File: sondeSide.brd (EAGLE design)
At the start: 127 x 31.8 mm, 33 parts

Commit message: I think its done, just needs labels
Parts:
- moved R2 6.37 mm to (42.4, 25.9), turned to 180 degrees
- moved R1 3.14 mm to (42.4, 23.4), turned to 180 degrees
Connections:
- net 3.3V: now also JP15.1
- net 5V: no longer U$1.UGND1, U$1.UGND2
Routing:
- net TX3: track 0.00 -> 68.8 mm
- net RX2: track 0.00 -> 63.0 mm
- net TX2: track 0.00 -> 62.5 mm
- net RX3: track 0.00 -> 61.0 mm
- net SCL: track 0.00 -> 54.3 mm
- net SDA: track 0.00 -> 50.7 mm
- net 3.3V: track 0.00 -> 32.7 mm
- net 12V: track 0.00 -> 27.5 mm

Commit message: I think its done
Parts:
- renumbered JP25 to VIN
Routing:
- net 3.3V: track 32.7 -> 105.5 mm
- net SCL: track 54.3 -> 40.7 mm
- net SDA: track 50.7 -> 51.2 mm
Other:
- board text added: "12V"
- board text added: "3.3V"
- board text added: "5V"
- board text added: "DEPTH"
- board text added: "GND"
- board text added: "RADIO"
- board text added: "RX"
- board text added: "RX2"
- board text added: "RX3"
- board text added: "SCL"
- board text added: "SDA"
- board text added: "SONDE"
- board text added: "TX"
- board text added: "TX2"
- board text added: "TX3"
- board text added: "V1 OCT 2018"

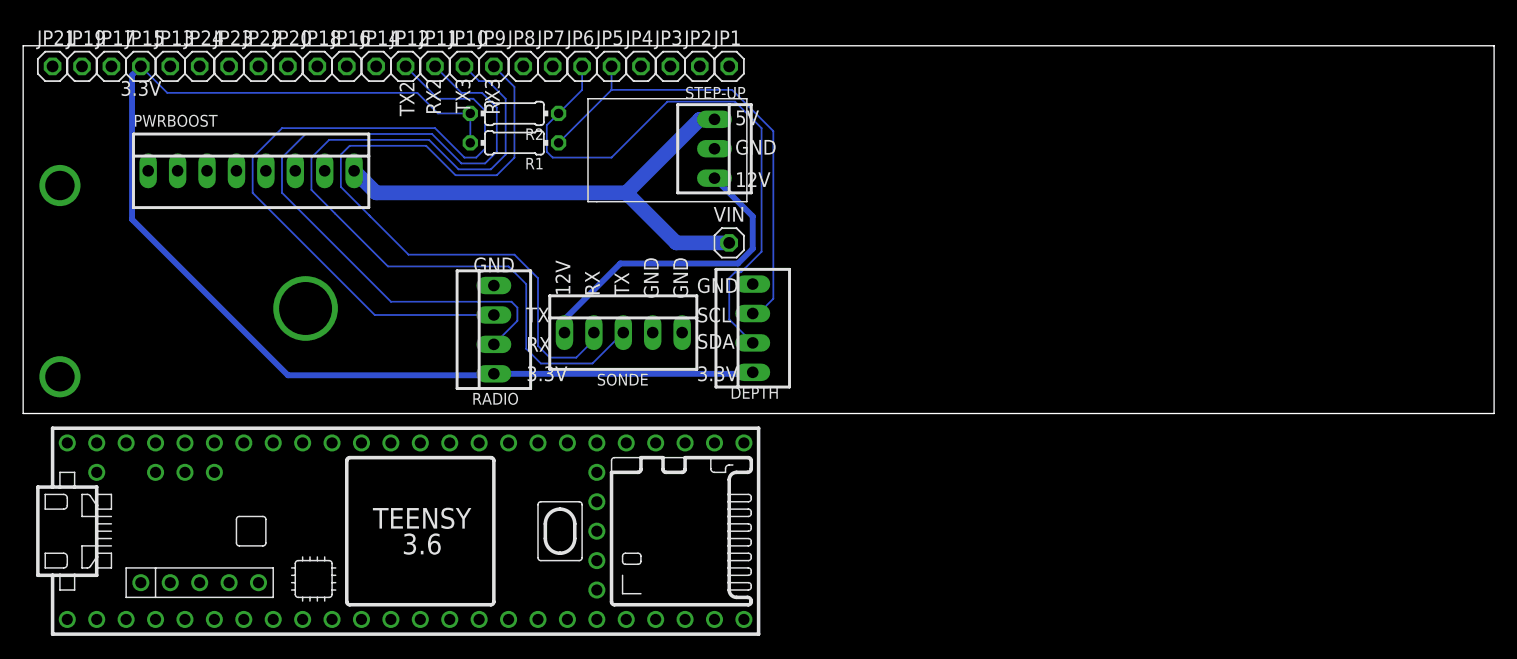
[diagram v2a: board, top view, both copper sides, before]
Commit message: Without external 3.3v step down
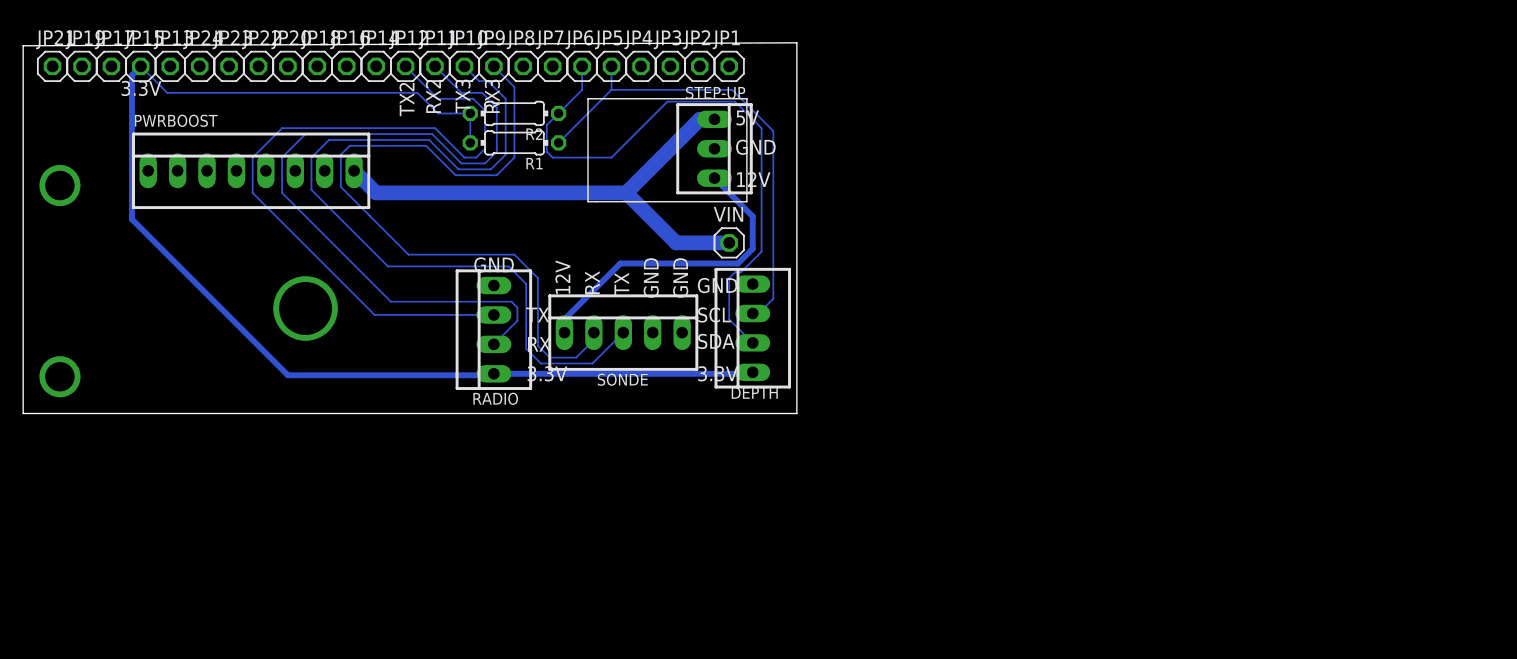
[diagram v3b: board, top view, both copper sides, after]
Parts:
- removed U$1: TEENSY_3.5/3.6, Teensy356:TEENSY_3.5/3.6
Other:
- board size 127 x 31.8 mm -> 66.8 x 32 mm
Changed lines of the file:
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@@
 <board>
 <plain>
-<wire x1="0" y1="0" x2="127" y2="0" width="0" layer="20"/>
-<wire x1="127" y1="0" x2="127" y2="31.75" width="0" layer="20"/>
-<wire x1="127" y1="31.75" x2="0" y2="31.75" width="0" layer="20"/>
+<wire x1="0" y1="0" x2="66.802" y2="0" width="0" layer="20"/>
+<wire x1="66.802" y1="0" x2="66.802" y2="32.004" width="0" layer="20"/>
+<wire x1="66.802" y1="32.004" x2="0" y2="31.75" width="0" layer="20"/>
 <wire x1="0" y1="31.75" x2="0" y2="0" width="0" layer="20"/>
 <wire x1="36.83" y1="27.94" x2="36.83" y2="13.081" width="0.025" layer="49"/>
@@
 <element name="JP24" library="pinhead" library_urn="urn:adsk.eagle:library:325" package="1X01" package3d_urn="urn:adsk.eagle:package:22485/2" value="" x="15.24" y="29.972"/>
 <element name="VIN" library="pinhead" library_urn="urn:adsk.eagle:library:325" package="1X01" package3d_urn="urn:adsk.eagle:package:22485/2" value="" x="60.96" y="14.732"/>
-<element name="U$1" library="Teensy356" package="TEENSY_3.5/3.6" value="TEENSY_3.5/3.6" x="31.75" y="-10.16"/>
 </elements>
 <signals>
@@
 </drawing>
 <compatibility>
-<note version="6.3" minversion="6.2.2" severity="warning">
-Since Version 6.2.2 text objects can contain more than one line,
-which will not be processed correctly with this version.
-</note>
 <note version="8.2" severity="warning">
 Since Version 8.2, EAGLE supports online libraries. The ids

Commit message: Pre-routing
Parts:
- removed VIN: (no value), pinhead:1X01
- added STEP-DOWN: 22-23-2041, con-molex:22-23-2041
- moved DEPTH 14.5 mm to (48.5, 7.11), turned to 270 degrees
- moved R1 9.16 mm to (51.1, 26.4)
- moved SONDE 7.64 mm to (59.4, 7.49), turned to 180 degrees
- moved STEP-UP 6.48 mm to (61.0, 16.5), turned to 0 degrees
- moved R2 1.14 mm to (41.4, 26.4)
- moved RADIO 0.18 mm to (40.8, 7.11), turned to 270 degrees
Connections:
- net 3.3V: now also STEP-DOWN.1
- net 5V: now also STEP-DOWN.3; no longer VIN.1
- net GND: now also STEP-DOWN.2
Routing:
- net 3.3V: track 105.5 -> 0.00 mm
- net TX3: track 68.8 -> 0.00 mm
- net RX2: track 63.0 -> 0.00 mm
- net TX2: track 62.5 -> 0.00 mm
- net RX3: track 61.0 -> 0.00 mm
- net SDA: track 51.2 -> 0.00 mm
- net 5V: track 45.2 -> 0.00 mm
- net SCL: track 40.7 -> 0.00 mm
- net 12V: track 27.4 -> 0.00 mm
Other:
- board text added: "Don't forget to cut VIN-VUSB!!"

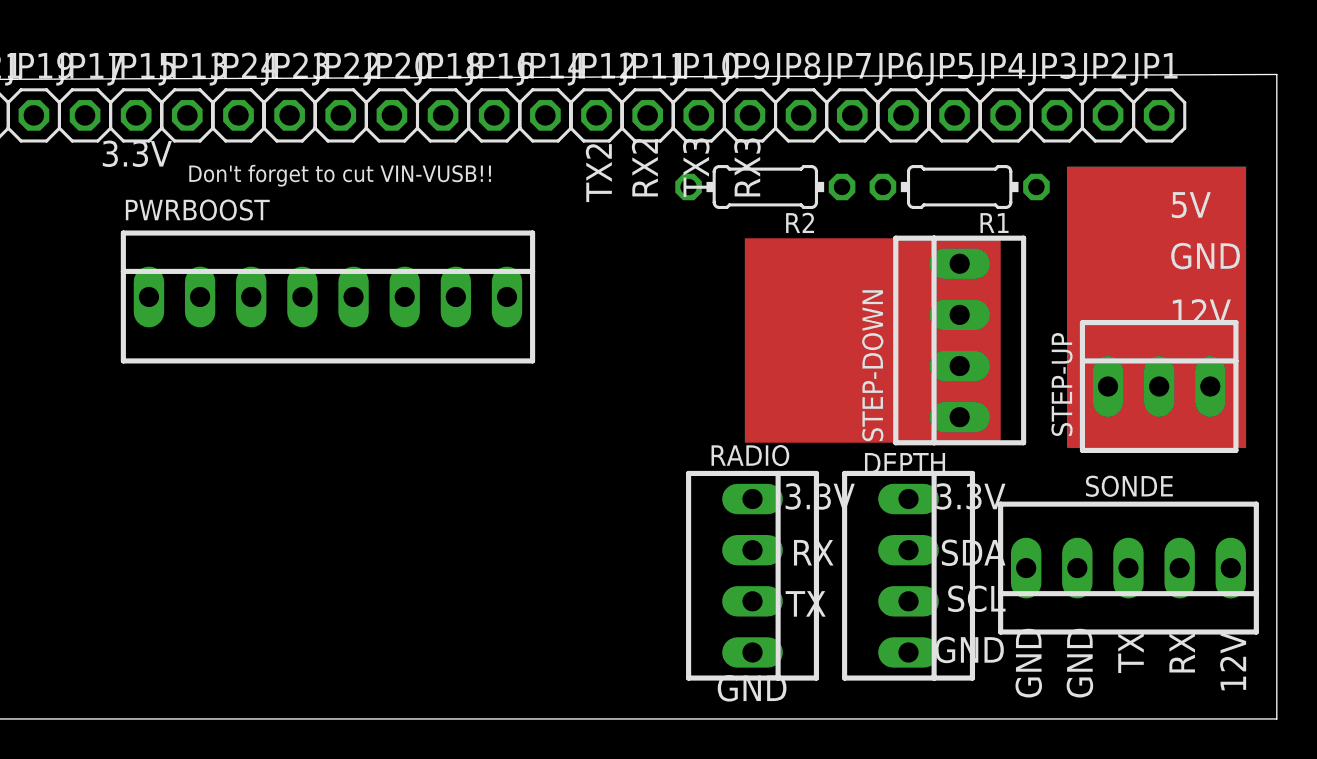
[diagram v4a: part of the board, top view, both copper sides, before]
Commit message: Everything but ground plane
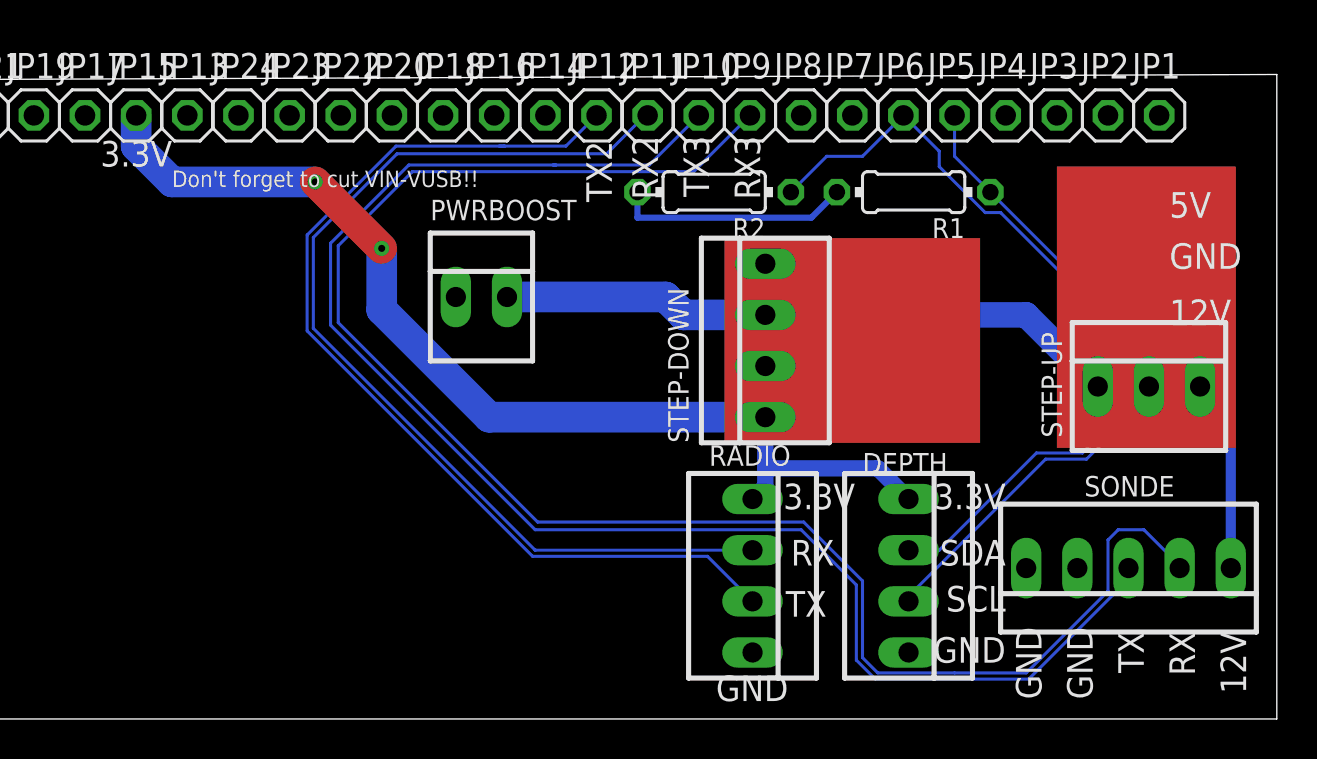
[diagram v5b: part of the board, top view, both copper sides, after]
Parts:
- PWRBOOST: value 22-23-2081 -> 22-23-2021; device con-molex:22-23-2081 -> con-molex:22-23-2021
- moved STEP-DOWN 9.65 mm to (41.4, 18.8)
- moved PWRBOOST 7.62 mm to (27.3, 21.0)
- moved R2 2.55 mm to (38.9, 26.2)
- moved R1 2.30 mm to (48.8, 26.2)
- moved STEP-UP 0.51 mm to (60.5, 16.5)
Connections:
- net 5V: now also PWRBOOST.2; no longer PWRBOOST.8
- net GND: now also PWRBOOST.1; no longer PWRBOOST.7
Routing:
- net RX3: track 0.00 -> 83.5 mm
- net TX3: track 0.00 -> 76.9 mm
- net 3.3V: track 0.00 -> 63.9 mm, vias 0 -> 2
- net RX2: track 0.00 -> 50.0 mm
- net TX2: track 0.00 -> 49.5 mm
- net SDA: track 0.00 -> 40.2 mm
- net SCL: track 0.00 -> 33.3 mm
- net 5V: track 0.00 -> 31.2 mm
- net 12V: track 0.00 -> 9.65 mm

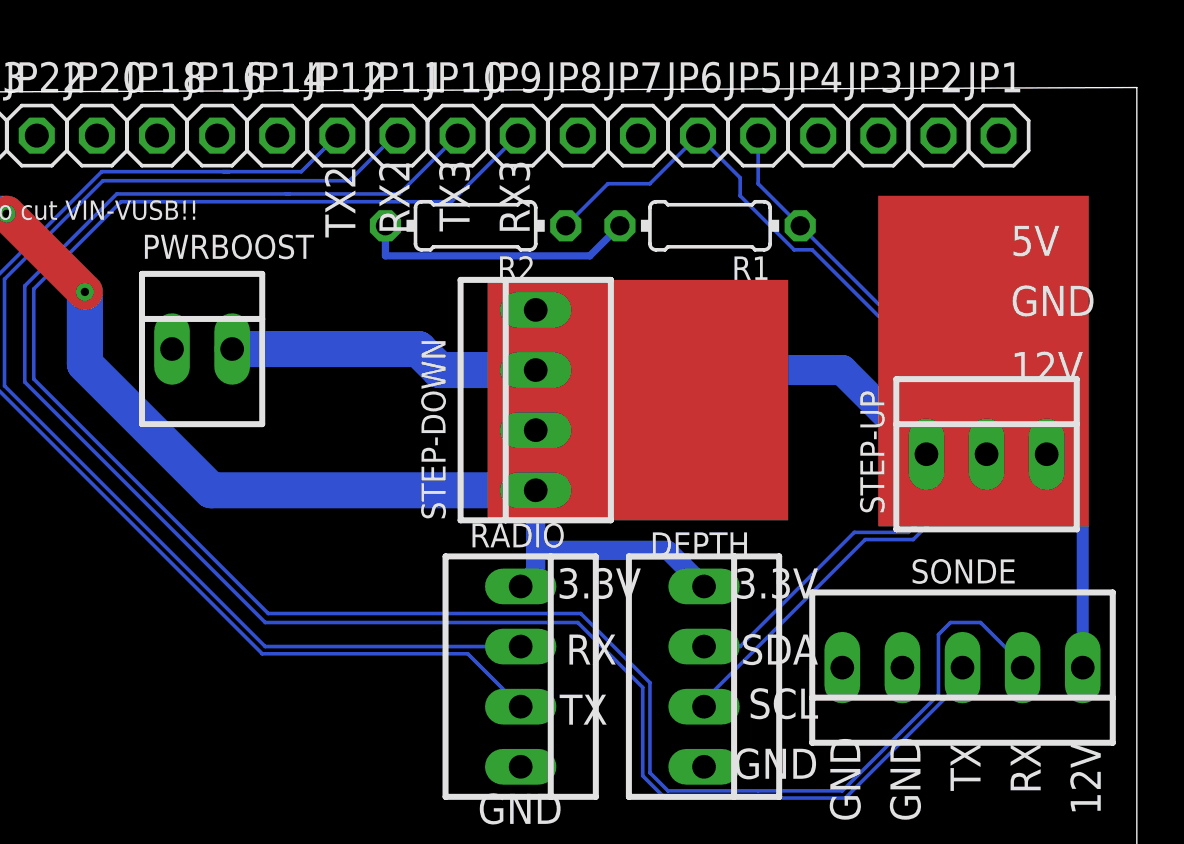
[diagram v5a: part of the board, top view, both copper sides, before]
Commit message: Looking good just need to add 500c holes
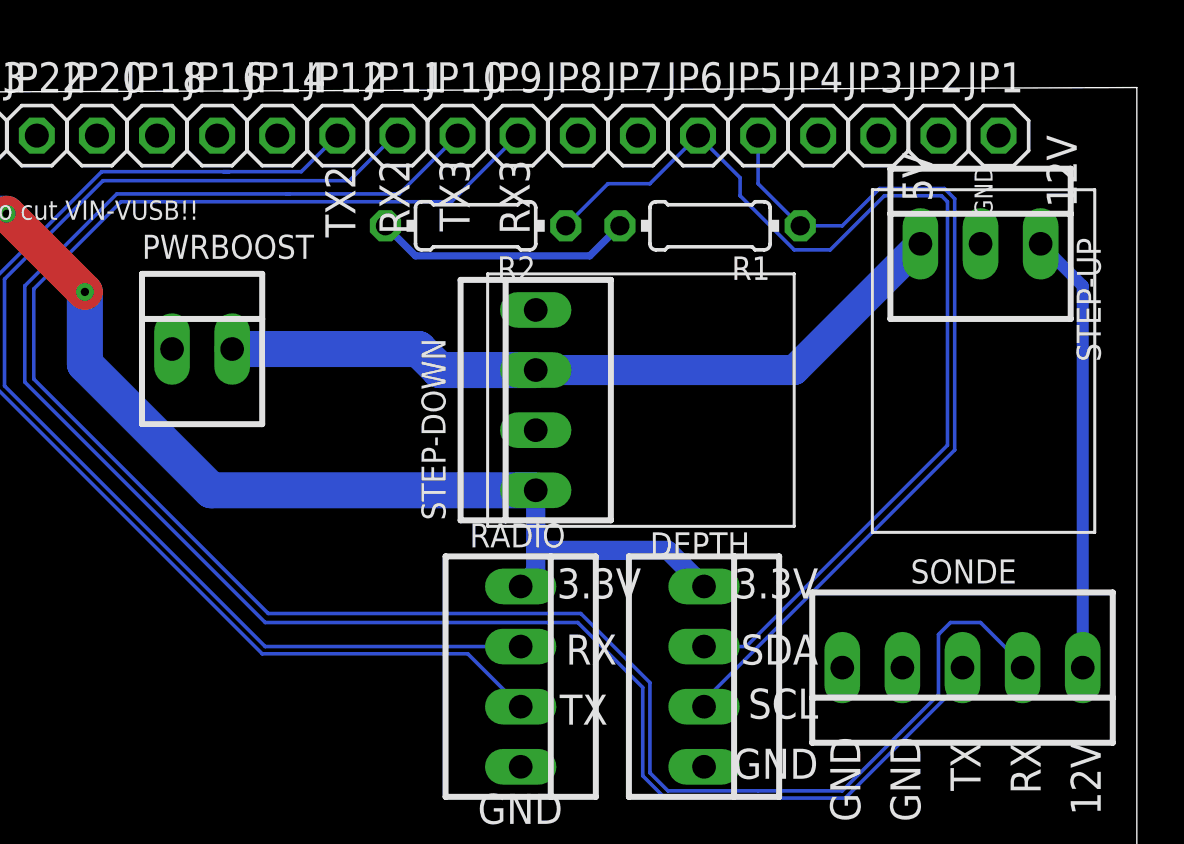
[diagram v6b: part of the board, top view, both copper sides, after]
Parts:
- moved STEP-UP 8.89 mm to (60.2, 25.4)
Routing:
- net 12V: track 9.65 -> 18.6 mm
- net SDA: track 40.2 -> 45.3 mm
- net SCL: track 33.3 -> 37.8 mm
- net 3.3V: track 63.9 -> 63.2 mm
